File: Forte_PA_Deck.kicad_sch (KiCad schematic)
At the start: 79 parts, among them J1 SMA, J2 5.08mm, J3 Keystone M5, J4 Keystone M5, J5 Conn_01x05, J6 Conn_Coaxial, Q1 MRF300AN, Q2 MRF300BN

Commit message: Add files via upload
Fixed DRC shorted nets error
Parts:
- added R5: 33, Resistor_SMD:R_2512_6332Metric, symbol Device:R_Small
- renumbered C19 to C10, C14 to C11, C15 to C12, C5 to C13, C20 to C14, C6 to C15, C21 to C16, C9 to C17, C32 to C18, C12 to C19, C33 to C20, C13 to C21, C34 to C22, C16 to C23, C35 to C24, C17 to C25, C22 to C26, C23 to C27, C24 to C28, C25 to C29, C7 to C3, C26 to C30, C27 to C31, C28 to C32, C29 to C33, C30 to C34, C31 to C35, C8 to C4, C10 to C5, C11 to C6, C3 to C7, C18 to C8, C4 to C9, D11 to D10, D10 to D11, L3 to L2, L2 to L3, L6 to L4, R5 to R4, R4 to R6
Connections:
- net To_GateA: now also R5.1
- net To_GateB: now also R5.2
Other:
- moved on the sheet: D5, R4

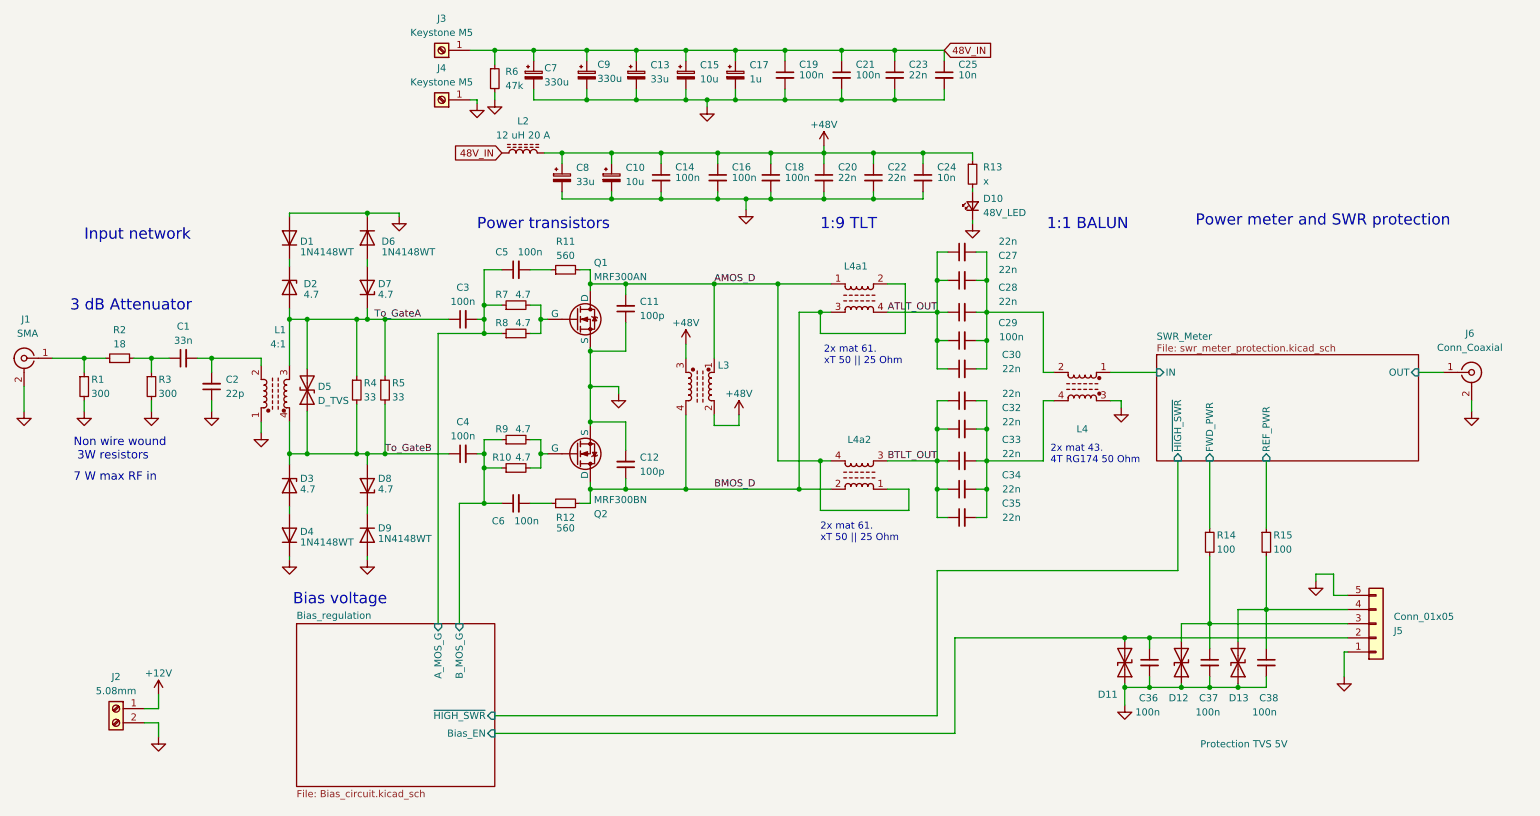
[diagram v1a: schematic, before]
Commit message: Used ERC on PA-Deck Schematic
Initially many hundreds of warnings, and some errors.
Apart from 8 exclusions These have all largely been fixed.
Many Symbols required updating from the appropriate library, but mostly a huge number or warnings about "symbol pin or wire end off grid connection".  Took a while, but I figured out what the problem is.
L5 & L6 exclusion referred to a TXRX library that wasn't available.
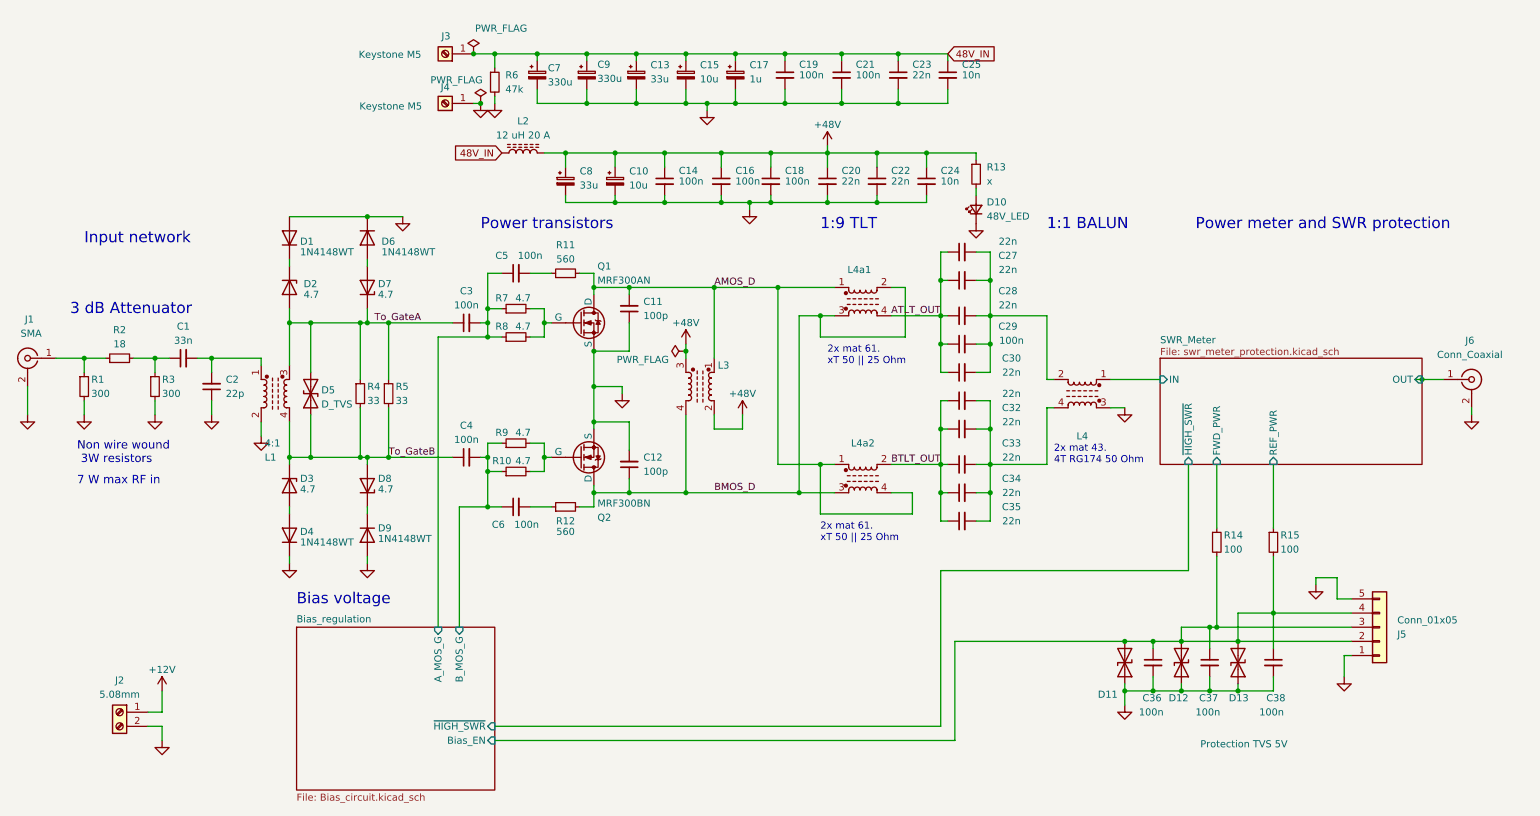
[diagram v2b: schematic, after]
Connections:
- net AMOS_D: now also Q1.1 (D); no longer Q1.3 (D)
- net BMOS_D: now also L4a2.3; no longer L4a2.2
- net BTLT_OUT: now also L4a2.2; no longer L4a2.3
- net Bias_regulation/Bias_EN: now also C37.1, C38.1, D12.2 (A2), D13.2 (A2), J5.3 (Pin_3), J5.4 (Pin_4), R14.2, R15.2
- net GND: now also L1.2, Q1.3 (S), Q2.3 (S); no longer L1.1, Q1.2 (S), Q2.2 (S)
- net at R10.2, R9.2: now also Q2.2 (G); no longer Q2.3 (G)
- net at R7.2, R8.2: now also Q1.2 (G); no longer Q1.1 (G)
- net at C1.2, C2.2: now also L1.1; no longer L1.2
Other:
- moved on the sheet: C10, C11, C12, C14, C16, C18, C20, C22, C23, C24, C25, C28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
